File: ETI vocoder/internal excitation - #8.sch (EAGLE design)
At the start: 51 parts, among them IC1 LM1458N, IC3 TL081P, IC4 UA741P, IC5 4006N, IC6 4030N, IC7 LM1458N, Q1 BC182L

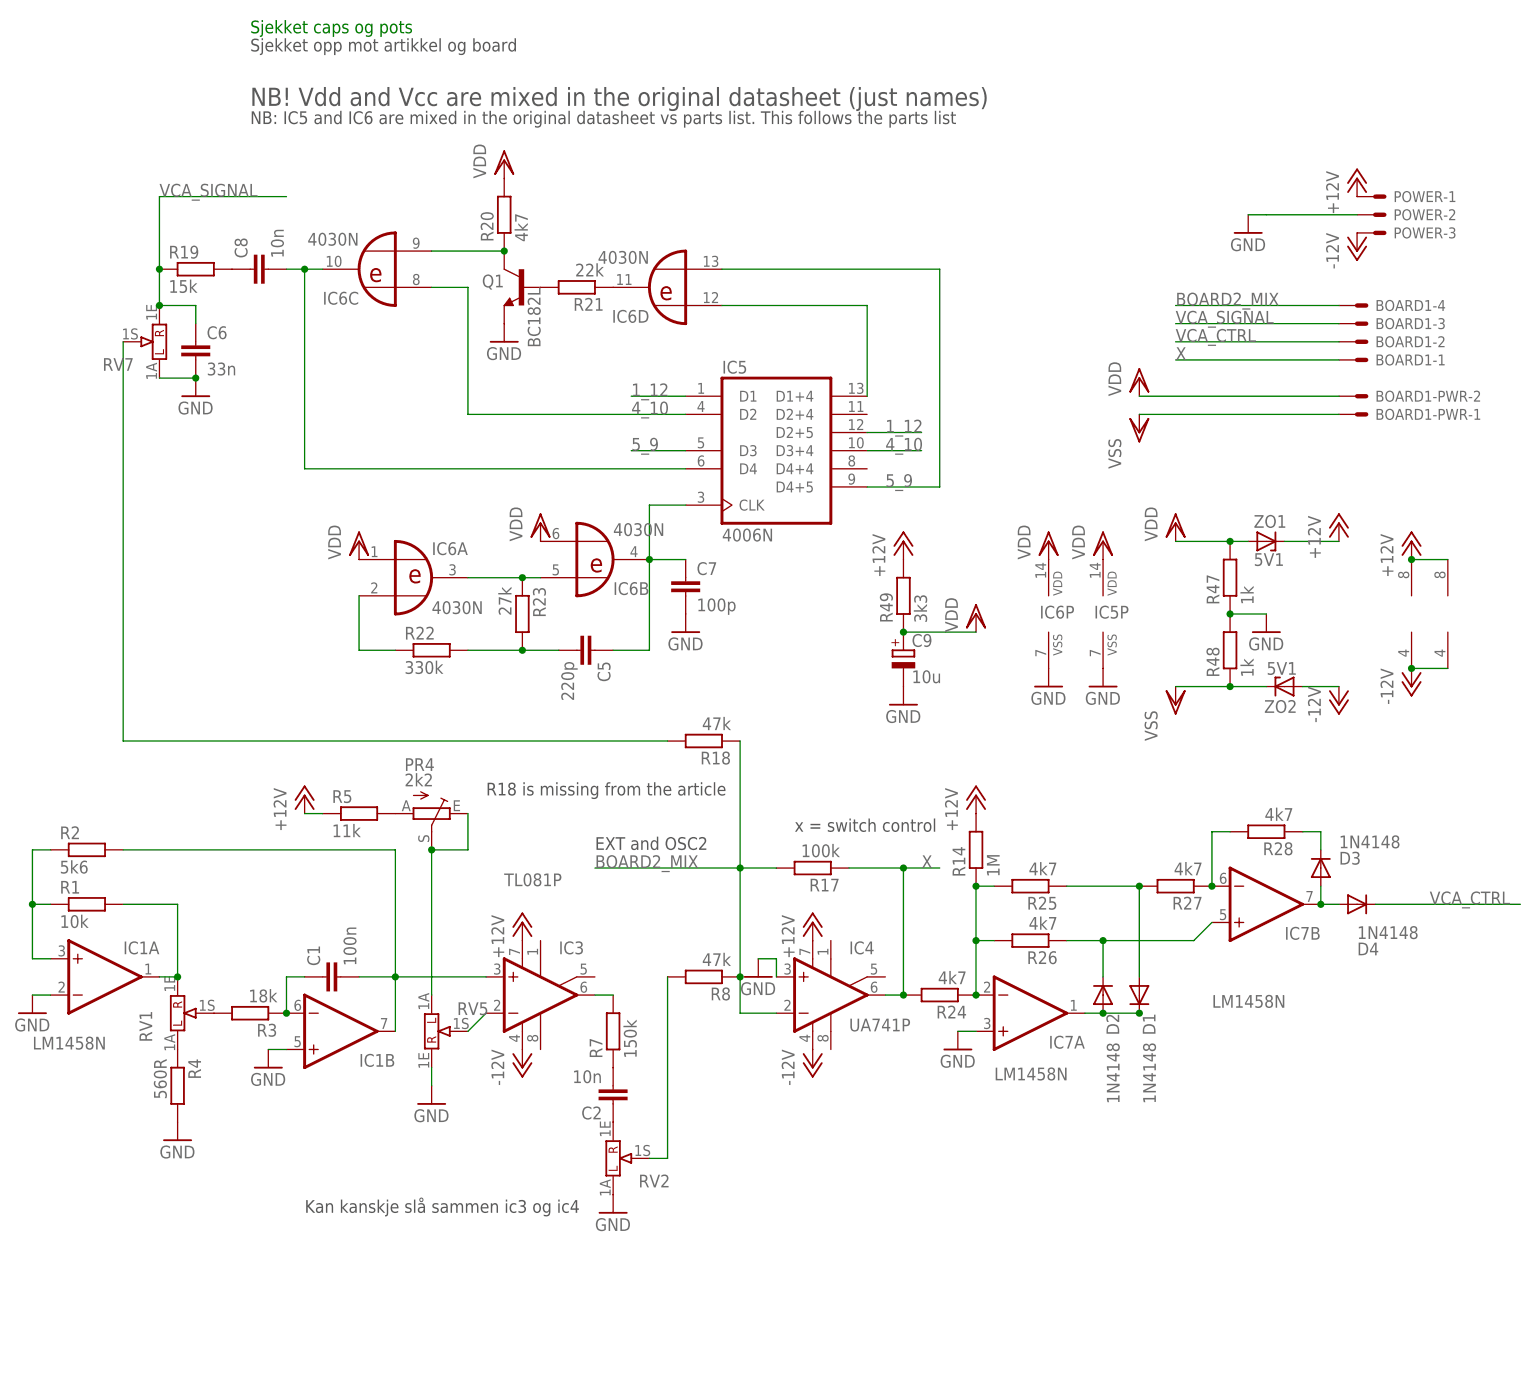
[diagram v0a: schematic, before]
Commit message: Fixed input boards in regards to article and added spacer holes
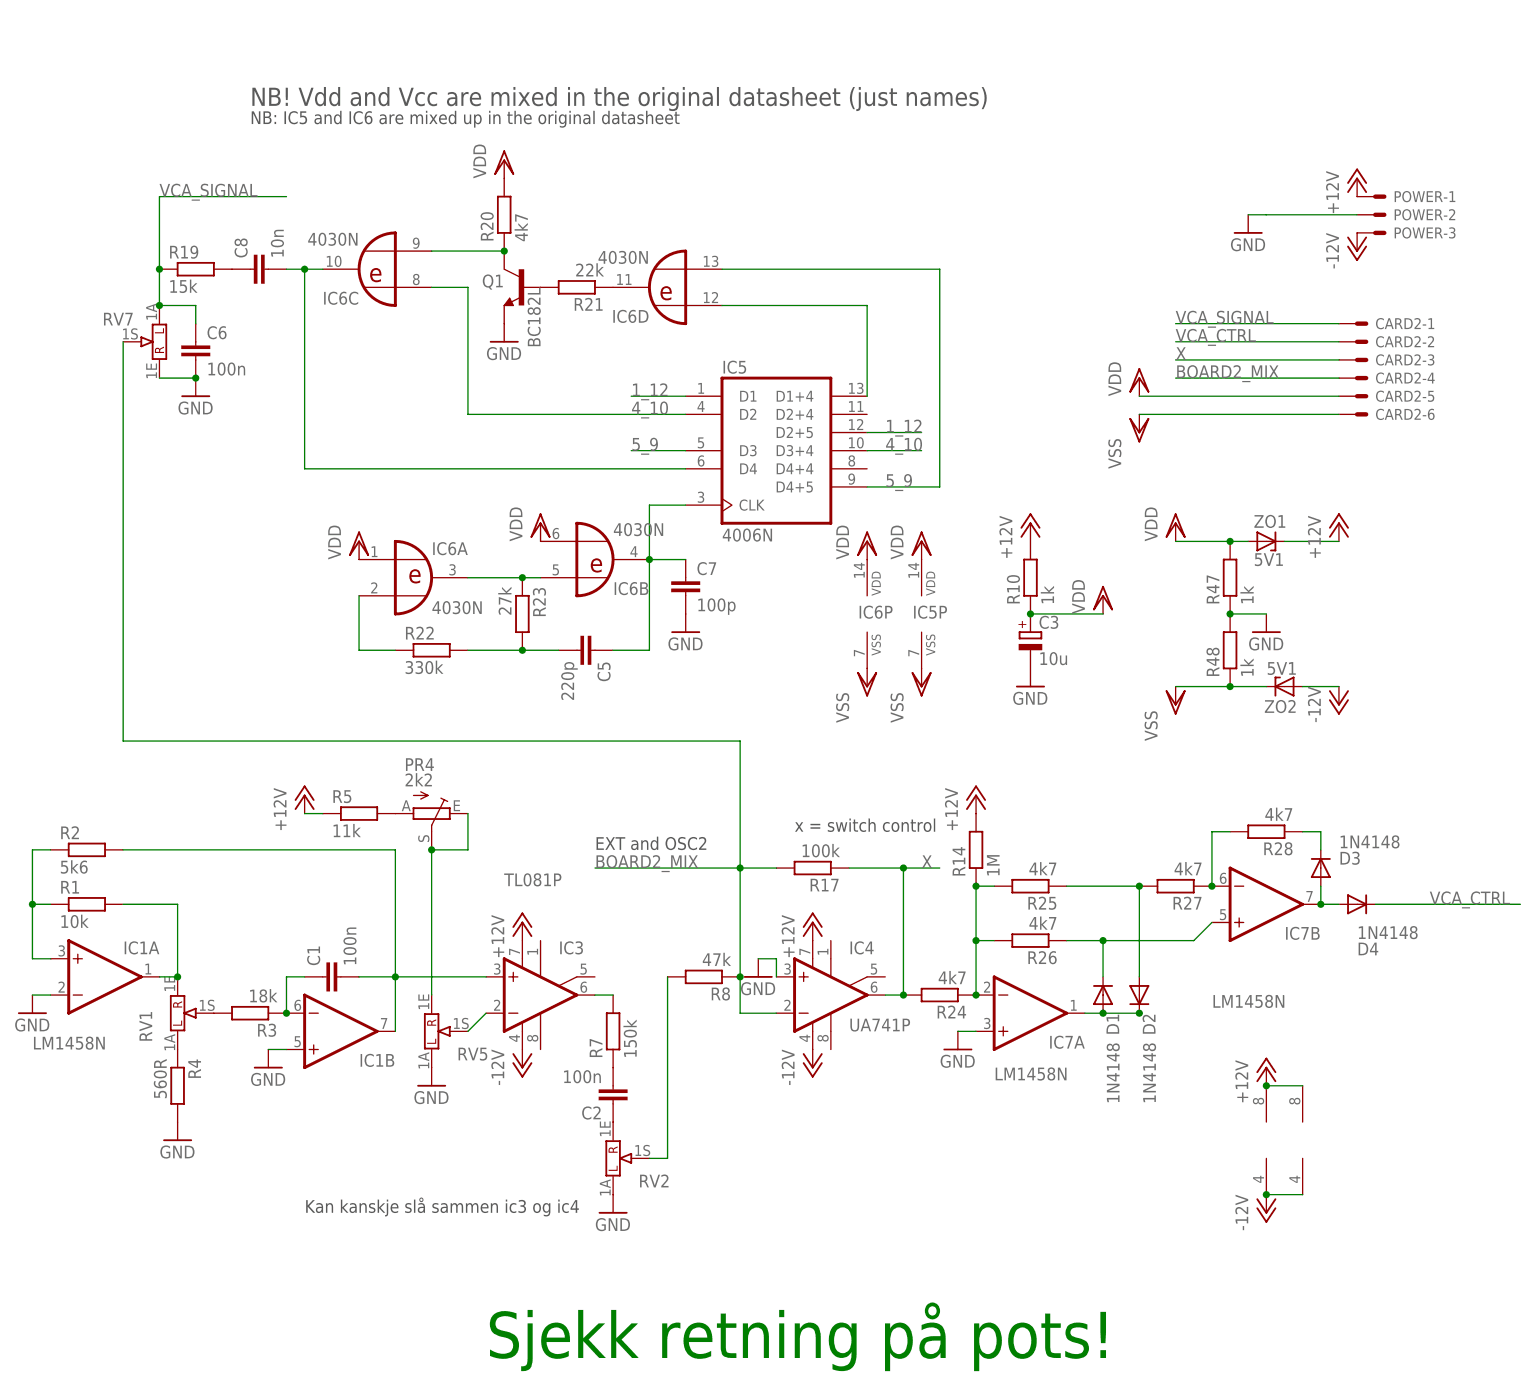
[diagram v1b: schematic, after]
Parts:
- removed BOARD1: 22-23-2041, con-molex:22-23-2041
- removed BOARD1-PWR: 22-23-2021, con-molex:22-23-2021
- removed C9: 10u, resistor:CPOL-EUE2.5-5
- removed R18: 47k, resistor:R-EU_0207/7
- removed R49: 3k3, resistor:R-EU_0207/7
- added C3: 10u, resistor:CPOL-EUE2.5-5
- added CARD2: (no value), con-molex:22-23-2061
- added R10: 1k, resistor:R-EU_0207/7
- C1, C8: device resistor:C-EU075-032X103 -> resistor:C-EU050-025X075
- C2: value 10n -> 100n
- C6: value 33n -> 100n; device resistor:C-EU075-032X103 -> resistor:C-EU025-025X050
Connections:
- removed net N$22: R18.2, RV7G$1.1S
- net +12V: now also R10.2; no longer R49.2
- net BOARD2_MIX: now also CARD2-4.S, RV7G$1.1S; no longer BOARD1-4.S, R18.1
- net GND: now also C3.-, RV5G$1.1A, RV7G$1.1E; no longer C9.-, IC5P.VSS, IC6P.VSS, RV5G$1.1E, RV7G$1.1A
- net N$15: now also D1.A, D2.C; no longer D1.C, D2.A
- net N$17: now also D1.C; no longer D2.C
- net N$18: now also D2.A; no longer D1.A
- net N$9: now also RV5G$1.1E; no longer RV5G$1.1A
- net VCA_CTRL: now also CARD2-2.S; no longer BOARD1-2.S
- net VCA_SIGNAL: now also CARD2-1.S, RV7G$1.1A; no longer BOARD1-3.S, RV7G$1.1E
- net VDD: now also C3.+, CARD2-5.S, R10.1; no longer BOARD1-PWR-2.S, C9.+, R49.1
- net VSS: now also CARD2-6.S, IC5P.VSS, IC6P.VSS; no longer BOARD1-PWR-1.S
- net X: now also CARD2-3.S; no longer BOARD1-1.S
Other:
- note added: "NB: IC5 and IC6 are mixed up in the original datasheet"
- note added: "Sjekk retning på pots!"
- note removed: "NB: IC5 and IC6 are mixed in the original datasheet vs parts list. This follows the parts list"
- note removed: "R18 is missing from the article"
- note removed: "Sjekket caps og pots"
- note removed: "Sjekket opp mot artikkel og board"
- moved on the sheet: D1, D2, IC5P, IC6P, RV5, RV7
